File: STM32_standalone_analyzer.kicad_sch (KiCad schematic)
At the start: 5 parts, among them U1 STM32F446RETx

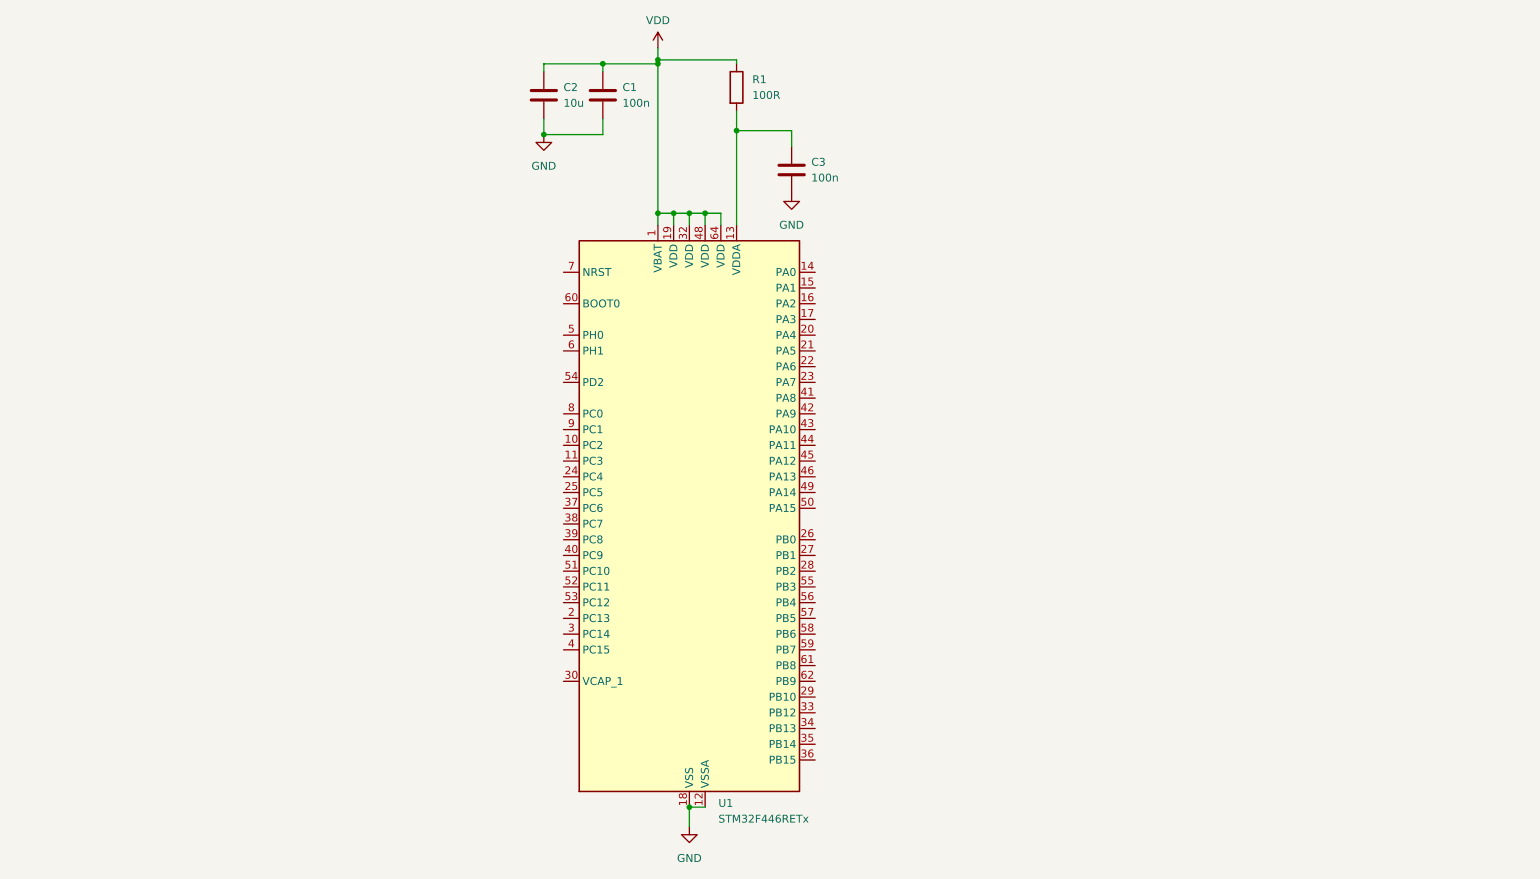
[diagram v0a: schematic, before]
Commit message: adding multiple sheets
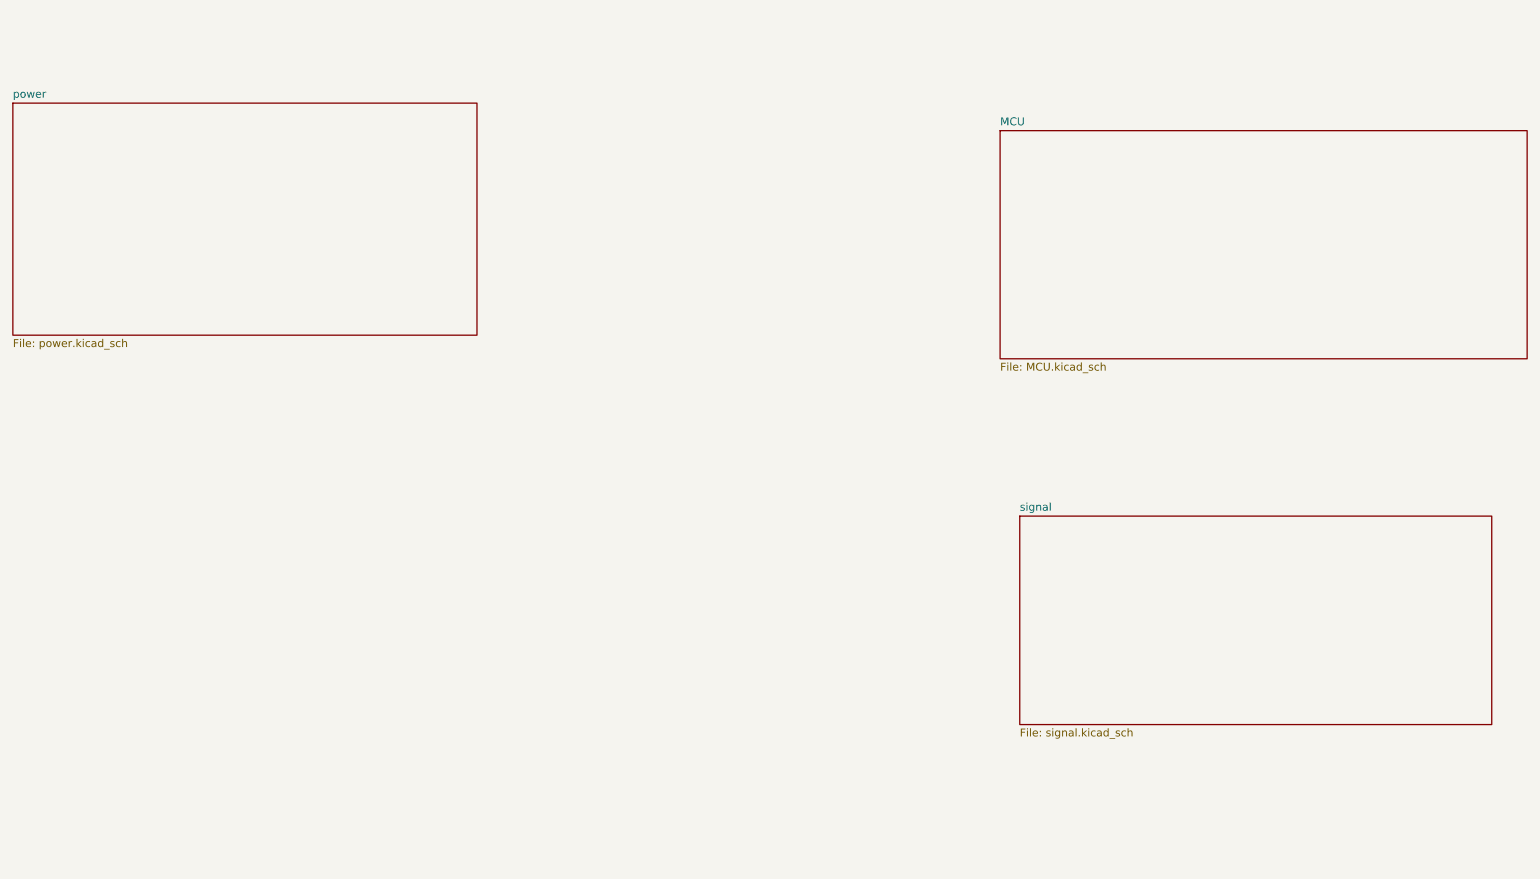
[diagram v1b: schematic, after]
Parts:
- removed C1, C3: 100n, symbol Device:C
- removed C2: 10u, symbol Device:C
- removed R1: 100R, symbol Device:R
- removed U1: STM32F446RETx, Package_QFP:LQFP-64_10x10mm_P0.5mm, symbol MCU_ST_STM32F4:STM32F446RETx
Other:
- added sheet MCU (MCU.kicad_sch)
- added sheet power (power.kicad_sch)
- added sheet signal (signal.kicad_sch)
